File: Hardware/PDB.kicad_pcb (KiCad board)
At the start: 2 copper layers, 47 x 32.8 mm, 50 parts, among them J1 Conn_01x02, J2 Conn_01x02, J3 Conn_01x02, J4 Conn_01x02, J5 Conn_01x02, Q1 Q_PMOS_GDS, U1 TPS54302, U2 TPS54302, U3 AP2112K-1.8, U4 INA219AxD

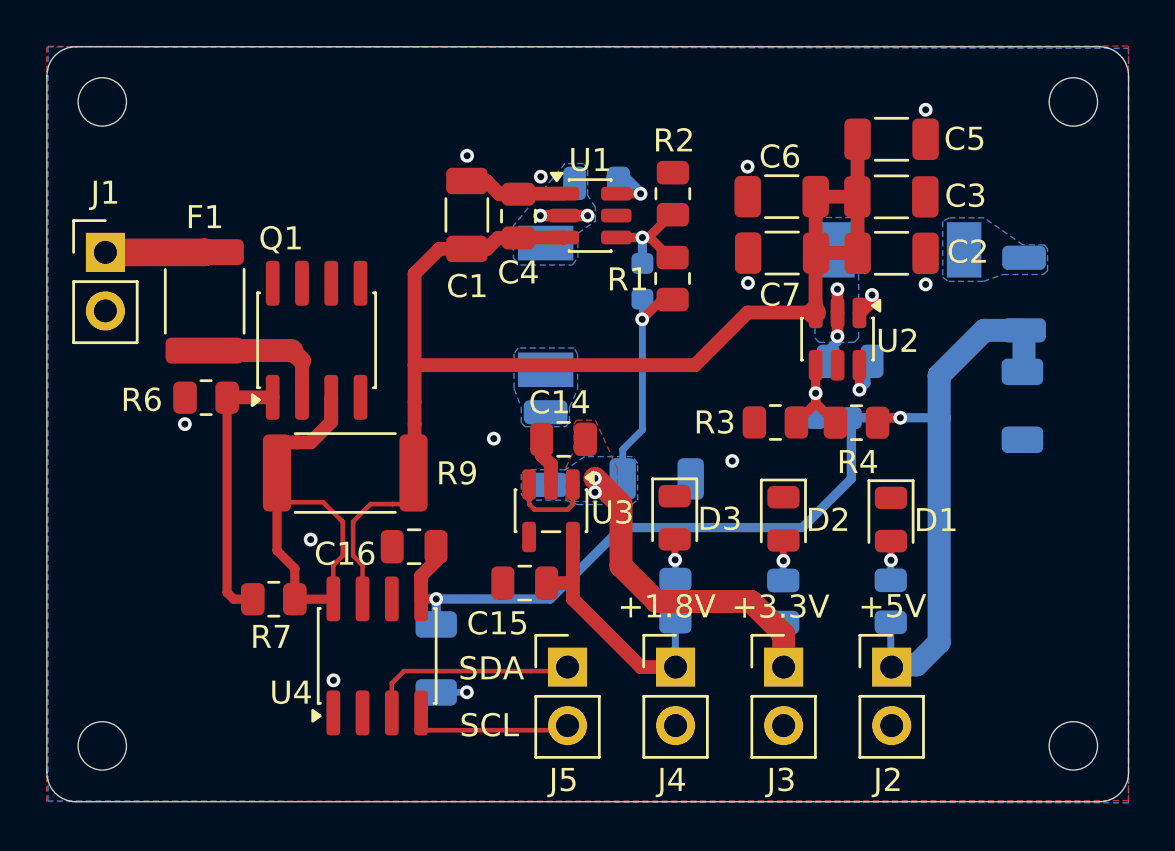
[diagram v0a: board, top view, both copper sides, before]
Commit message: Added silkscreen labels
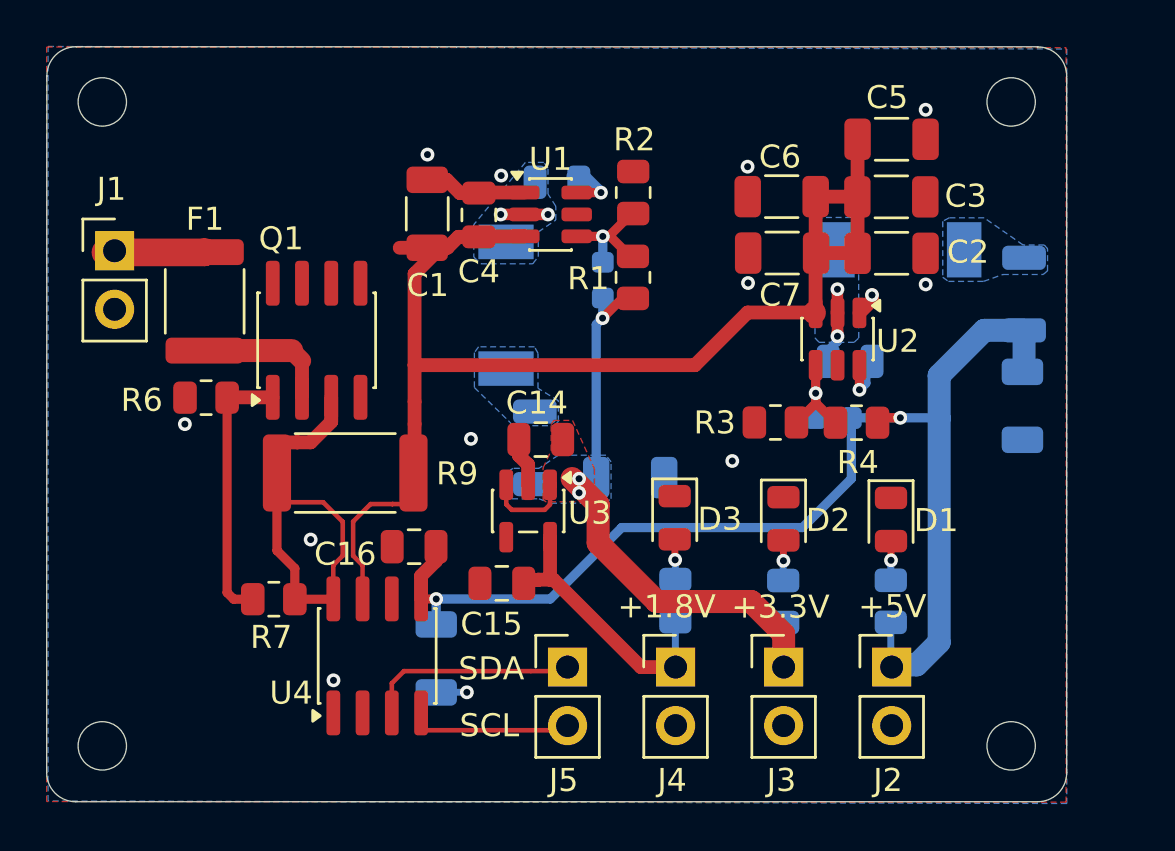
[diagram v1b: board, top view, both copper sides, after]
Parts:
- moved H2 2.70 mm to (70.0, 58.7)
- moved H4 2.70 mm to (70.0, 86.7)
- moved C8 1.72 mm to (50.3, 62.2)
- moved C1 1.72 mm to (44.7, 63.6)
- moved C11 1.72 mm to (52.3, 66.4)
- moved C4 1.72 mm to (46.9, 63.6)
- moved L1 1.72 mm to (48.1, 67.5)
- moved R1 1.72 mm to (53.6, 66.3)
- moved R2 1.72 mm to (53.6, 62.6)
- moved U1 1.72 mm to (50.0, 63.6)
- moved C10 1.15 mm to (53.5, 75.0)
- moved U3 0.99 mm to (49.0, 76.5)
- moved C14 0.99 mm to (49.6, 73.4)
- moved C15 0.99 mm to (47.9, 79.6)
- moved L2 0.47 mm to (49.3, 73.7)
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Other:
- board size 47 x 32.8 mm -> 44.3 x 32.8 mm

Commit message: Small fixes
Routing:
- net +BATT: track 45.2 -> 44.4 mm
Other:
- board text added: "+"
- board text added: "-"
- board text added: "BATT"
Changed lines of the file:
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@@
 		(tags "resistor")
 		(property "Reference" "R4"
-			(at 3.5775 1.7325 180)
+			(at 6.5275 0.1725 180)
 			(layer "F.SilkS")
 			(effects
@@
 		(tags "resistor")
 		(property "Reference" "R6"
-			(at -2.79 0.11 0)
+			(at 0.83 1.75 0)
 			(layer "F.SilkS")
 			(effects
@@
 		)
 	)
+	(gr_text "+"
+		(at 28.265 65.725 0)
+		(layer "F.SilkS")
+		(effects
+			(font
+				(size 1 1)
+				(thickness 0.15)
+			)
+			(justify left bottom)
+		)
+	)
 	(gr_text "+5V"
 		(at 63.365 81.185 0)
@@
 		)
 	)
+	(gr_text "BATT"
+		(at 29.255 70.775 0)
+		(layer "F.SilkS")
+		(effects
+			(font
+				(size 1 1)
+				(thickness 0.15)
+			)
+			(justify left bottom)
+		)
+	)
+	(gr_text "-"
+		(at 28.215 68.235 0)
+		(layer "F.SilkS")
+		(effects
+			(font
+				(size 1 1)
+				(thickness 0.15)
+			)
+			(justify left bottom)
+		)
+	)
 	(gr_text "+3.3V"
 		(at 57.855 81.205 0)
@@
 	)
 	(segment
-		(start 44.105 70.125)
-		(end 44.105 66.155)
+		(start 45.13 65.03)
+		(end 45.18 65.08)
 		(width 0.6)
 		(layer "F.Cu")
@@
 	)
 	(segment
+		(start 44.105 65.58)
+		(end 44.655 65.03)
+		(width 0.6)
+		(layer "F.Cu")
+		(net 1)
+	)
+	(segment
 		(start 61.515 62.81)
 		(end 63.315 62.81)
@@
 	)
 	(segment
+		(start 44.105 70.125)
+		(end 44.105 65.58)
+		(width 0.6)
+		(layer "F.Cu")
+		(net 1)
+	)
+	(segment
 		(start 56.275 70.125)
 		(end 44.105 70.125)
@@
 	)
 	(segment
-		(start 44.105 66.155)
-		(end 45.18 65.08)
+		(start 44.655 65.03)
+		(end 45.13 65.03)
 		(width 0.6)
 		(layer "F.Cu")
@@
 		(width 0.6)
 		(layer "F.Cu")
-		(net 1)
-	)
-	(segment
-		(start 43.46 65.03)
-		(end 44.655 65.03)
-		(width 0.6)
-		(layer "F.Cu")

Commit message: More small changes
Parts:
- moved C10 0.27 mm to (53.7, 75.0)
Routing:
- net GND: vias 13 -> 14
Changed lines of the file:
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@@
 	(footprint "Capacitor_SMD:C_1206_3216Metric"
 		(layer "B.Cu")
-		(at 53.465 75.005)
+		(at 53.735 75.035)
 		(descr "Capacitor SMD 1206 (3216 Metric), square (rectangular) end terminal, IPC-7351 nominal, (Body size source: IPC-SM-782 page 76, https://www.pcb-3d.com/wordpress/wp-content/uploads/ipc-sm-782a_amendment_1_and_2.pdf), generated with kicad-footprint-generator")
 		(tags "capacitor")
@@
 	)
 	(via
+		(at 70.485 74.365)
+		(size 0.6)
+		(drill 0.3)
+		(layers "F.Cu" "B.Cu")
+		(net 2)
+	)
+	(via
 		(at 66.289759 66.619827)
 		(size 0.6)
@@
 		(layer "B.Cu")
 		(hatch edge 0.5)
-		(priority 2)
+		(priority 7)
 		(connect_pads yes
 			(clearance 0.25)
@@
 		(polygon
 			(pts
-				(xy 61.835 63.715502) (xy 61.495 63.935502) (xy 61.485 68.945) (xy 61.665 69.135) (xy 63.185 69.135502)
-				(xy 63.385 68.945) (xy 63.375 63.905502) (xy 63.055 63.715502)
+				(xy 61.495 63.935502) (xy 61.835 63.715502) (xy 63.055 63.715502) (xy 63.375 63.905502) (xy 63.385 66.385)
+				(xy 62.945 66.875) (xy 62.945 68.945) (xy 62.655 69.405) (xy 62.655 70.585) (xy 62.465 70.775) (xy 61.665 70.775)
+				(xy 61.475 70.605)
 			)
 		)
@@
 		(polygon
 			(pts
-				(xy 52.634658 74.325) (xy 52.415 74.035) (xy 50.335 74.035) (xy 49.504658 74.605) (xy 48.374658 74.605)
+				(xy 52.974658 74.325) (xy 52.755 74.035) (xy 50.335 74.035) (xy 49.504658 74.605) (xy 48.374658 74.605)
 				(xy 48.114658 74.785) (xy 48.114658 75.665) (xy 48.334658 75.925) (xy 49.504658 75.925) (xy 50.024658 76.115)
-				(xy 52.364658 76.115) (xy 52.635 75.925)
+				(xy 52.704658 76.115) (xy 52.975 75.925)
 			)
 		)

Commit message: More changes
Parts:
- removed L2, L4: 1uH, Inductor_SMD:L_1206_3216Metric
- added C18: 47uF, Capacitor_SMD:C_1206_3216Metric, B.Cu at (47.2, 73.9)
- added C19: 10uF, Capacitor_SMD:C_1206_3216Metric, B.Cu at (70.1, 70.9)
- added FB1: FerriteBead, Inductor_SMD:L_0805_2012Metric, B.Cu at (49.3, 73.4)
- added FB2: FerriteBead, Inductor_SMD:L_0805_2012Metric, B.Cu at (70.0, 66.6)
- C10: value 47uF -> 10uF
- moved C12 9.44 mm to (70.3, 62.5), turned to 90 degrees
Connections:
- C12 pad 1: +5V -> Net-(C12-Pad1)
- L3 pad 2: Net-(L3-Pad2) -> Net-(C12-Pad1)
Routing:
- added copper zone on B.Cu, net Net-(C12-Pad1)
- removed copper zone on B.Cu, net Net-(L3-Pad2)

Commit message: More changes
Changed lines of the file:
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@@
 		(tags "capacitor")
 		(property "Reference" "C7"
-			(at 0.085 -1.825 180)
+			(at 3.467 0.061 180)
 			(layer "F.SilkS")
 			(effects
@@
 		(tags "capacitor")
 		(property "Reference" "C6"
-			(at 0.075 1.725 0)
+			(at 3.447 -0.103 0)
 			(layer "F.SilkS")
 			(effects
@@
 		(tags "capacitor")
 		(property "Reference" "C5"
-			(at -0.195 -1.815 180)
+			(at -3.391 0.053 180)
 			(layer "F.SilkS")
 			(effects
@@
 		(tags "Choke SMD")
 		(property "Reference" "L3"
-			(at -4.415 -2.325 180)
+			(at -2.521 -3.985 180)
 			(layer "B.SilkS")
 			(effects
